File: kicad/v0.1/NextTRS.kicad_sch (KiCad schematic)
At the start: 62 parts, among them J1 TRS-80 M3 Pin Header, J10 DB15_Female_HighDensity, J2 TRS-80 M1 Pin Connector, J3 TRS-80 M3 Edge Connector, J4 TRS-80 M1 Edge Connector, J5 AudioJack3, J6 Mini-DIN-6, J7 USB_B_Micro, J8 SD_Card, J9 Programmer, Q1 2N7002, Q2 2N7002, Q3 2N7002, Q4 MMBT3904, Q5 MMBT3904, SW1 SW_DIP_x04, SW2 SW_Push, SW3 SW_Push, SW4 ESP_RESET, SW5 PTRS_RESET, U1 ESP32-WROVER-B, U2 74LVC245, U3 74LVC245, U4 MCP43x1, U5 74LVC245, U6 74LVC245, U7 74LVC245

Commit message: Do not use Bank 4 (1.5V)
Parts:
- added C11: 0.1uF, Capacitor_SMD:C_0805_2012Metric_Pad1.18x1.45mm_HandSolder, symbol Device:C
- renumbered C5 to C1, C6 to C2, C1 to C3, C2 to C4, C8 to C5, C3 to C6, C4 to C7, C7 to C8, J9 to J5, J8 to J6, J5 to J7, J6 to J8, J7 to J9, R11 to R1, R1 to R10, R2 to R11, R3 to R12, R4 to R13, R18 to R14, R19 to R15, R17 to R16, R5 to R17, R6 to R18, R14 to R19, R12 to R2, R13 to R3, R7 to R4, R8 to R5, R15 to R6, R16 to R7, R9 to R8, R10 to R9, SW3 to SW1, SW4 to SW2, SW5 to SW3, SW2 to SW4, SW1 to SW5, U5 to U4, U6 to U5, U7 to U6, U4 to U7
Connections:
- net +3V3: now also C11.2
- net GND: now also C11.1
- net INT_OUT_N: now also Conn1.182 (D10); no longer Conn1.158 (E9)
- net WAIT_OUT_N: now also Conn1.180 (D11); no longer Conn1.160 (E8)

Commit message: Add hires interface for the M3
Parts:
- added C1: 100, Capacitor_SMD:C_0805_2012Metric_Pad1.18x1.45mm_HandSolder, symbol Device:C
- added J5, J6: Conn_01x06_Male, Connector_PinHeader_2.54mm:PinHeader_1x06_P2.54mm_Horizontal, symbol Connector:Conn_01x06_Male
- added R10, R8, R9: 10K, Resistor_SMD:R_0805_2012Metric_Pad1.20x1.40mm_HandSolder, symbol Device:R
- added R4, R5, R6, R7: 4K7, Resistor_SMD:R_0805_2012Metric_Pad1.20x1.40mm_HandSolder, symbol Device:R
- renumbered C9 to C10, C10 to C11, C11 to C12, C3 to C2, C4 to C3, C6 to C4, C7 to C5, C1 to C6, C2 to C7, C5 to C8, C8 to C9, J8 to J10, J9 to J11, J10 to J12, J5 to J8, J6 to J9, R10 to R11, R11 to R12, R12 to R13, R13 to R14, R4 to R15, R5 to R16, R8 to R17, R9 to R18, R6 to R19, R7 to R20, R14 to R21, R15 to R22, R16 to R23, R17 to R24, R18 to R25, R19 to R26, SW5 to SW1, SW1 to SW2, SW2 to SW3, SW3 to SW4, SW4 to SW5
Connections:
- net +3.3V: now also R4.1, R5.1, R6.1, R7.1
- net CONF_1: now also Conn1.153 (A6), R4.2; no longer Conn1.192 (R7)
- net CONF_2: now also Conn1.149 (A7), R5.2; no longer Conn1.194 (P7)
- net CONF_3: now also Conn1.147 (C6), R6.2; no longer Conn1.198 (M6)
- net CONF_4: now also Conn1.143 (B8), R7.2; no longer Conn1.200 (L8)
- net GND: now also C1.2, J5.1 (Pin_1), J5.3 (Pin_3), J5.5 (Pin_5), J6.1 (Pin_1), J6.3 (Pin_3), J6.5 (Pin_5), R10.2, R8.2, R9.2
- net VIDEOX: now reaches U5.13 (B5)
- net VIDEOX: now also Conn1.198 (M6)
- net VSYNCX: now reaches U5.14 (B4)
- net VSYNCX: now also Conn1.194 (P7)
- net HSYNCX: now reaches U5.15 (B3)
- net HSYNCX: now also Conn1.192 (R7)
- net HSYNC: now reaches U5.5 (A3)
- net HSYNC: now also J5.6 (Pin_6), R8.1
- net VSYNC: now reaches U5.6 (A4)
- net VSYNC: now also J5.4 (Pin_4), R9.1
- net VIDEO: now reaches U5.7 (A5)
- net VIDEO: now also J5.2 (Pin_2), R10.1
- net HSYNC_O: now reaches Conn1.183 (R9)
- net HSYNC_O: now also J6.6 (Pin_6)
- net VSYNC_O: now reaches Conn1.191 (N8)
- net VSYNC_O: now also J6.4 (Pin_4)
- net VIDEO_O: now reaches Conn1.193 (L9)
- net VIDEO_O: now also C1.1, J6.2 (Pin_2)
- no-connect marks 5 -> 13
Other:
- moved on the sheet: C2, C3, C4, C5, J10, J7, J9, R11, R12, R13, R14, R15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

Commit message: Add HDMI connector
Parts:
- removed C12: 0.1uF, Capacitor_SMD:C_0805_2012Metric_Pad1.18x1.45mm_HandSolder, symbol Device:C
- removed D1: LED_RCBG, LED_THT:LED_D5.0mm-4_RGB, symbol TRS-IO-M1-rescue:LED_RCBG-Device
- removed J12: DB15_Female_HighDensity, PocketTRS_Connectors:DB_15F-VGA, symbol Connector:DB15_Female_HighDensity
- removed SW2, SW5: SW_Push, Button_Switch_THT:SW_PUSH_6mm, symbol Switch:SW_Push
- removed U7: MCP43x1, Package_SO:TSSOP-20_4.4x6.5mm_P0.65mm, symbol MCP43X1:MCP43x1
- added C1, C2, C3, C4, C5, C6, C7, C8: 100n, Capacitor_SMD:C_0805_2012Metric_Pad1.18x1.45mm_HandSolder, symbol Device:C
- added D1: LED_RKBG, LED_THT:LED_D5.0mm-4_RGB, symbol Device:LED_RKBG
- added J7: HDMI_A, Connector_HDMI:HDMI_A_Molex_208658-1001_Horizontal, symbol Connector:HDMI_A
- added R10, R11, R4, R5, R6, R7, R8, R9: 50, Resistor_SMD:R_0805_2012Metric_Pad1.20x1.40mm_HandSolder, symbol Device:R
- added R28, R29: 4K7, Resistor_SMD:R_0805_2012Metric_Pad1.20x1.40mm_HandSolder, symbol Device:R
- J1: footprint Connector_PinSocket_2.54mm:PinSocket_2x25_P2.54mm_Vertical -> Connector_PinHeader_2.54mm:PinHeader_2x25_P2.54mm_Vertical
- J2: footprint Connector_PinSocket_2.54mm:PinSocket_2x20_P2.54mm_Vertical -> Connector_PinHeader_2.54mm:PinHeader_2x20_P2.54mm_Vertical
- renumbered C6 to C10, C7 to C11, C2 to C12, C3 to C13, C4 to C14, C5 to C15, C8 to C16, C9 to C17, C10 to C18, C11 to C19, C1 to C9, J7 to J10, J10 to J11, J11 to J12, Q4 to Q1, Q5 to Q2, Q1 to Q3, Q2 to Q4, Q3 to Q5, R8 to R12, R9 to R13, R10 to R14, R11 to R21, R12 to R22, R13 to R23, R14 to R24, R21 to R25, R22 to R27, R23 to R30, R24 to R31, R25 to R32, R4 to R33, R5 to R34, R6 to R35, R7 to R36, SW3 to SW1, SW4 to SW2, SW1 to SW3
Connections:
- net PTRS_RESET is gone; now on net BUTTON: R30.2, SW2.2, U1.7 (IO35)
- net VGA_BLUE is gone; now on net _A12: Conn1.34 (P16)
- net VGA_GREEN is gone; now on net _A10: Conn1.30 (P15)
- net VGA_HSYNC is gone; now on net _A15: Conn1.40 (N16)
- net VGA_VSYNC is gone; now on net _A13: Conn1.36 (N15)
- net +3.3V: now also R25.1, R27.1, R30.1, R10.1, R11.1, R4.1, R5.1, R6.1, R7.1, R8.1, R9.1; no longer R26.1
- net +3V3: now also R26.1, R28.1, R29.1; no longer R25.1, R27.1, R30.1, U5.1 (A->B)
- net A0: now also U2.9 (A7); no longer U2.2 (A0)
- net A1: now also U2.8 (A6); no longer U2.3 (A1)
- net A10: now also U4.18 (B0); no longer U4.4 (A2)
- net A11: now also U4.13 (B5); no longer U4.5 (A3)
- net A12: now also U4.17 (B1); no longer U4.6 (A4)
- net A13: now also U4.16 (B2); no longer U4.7 (A5)
- net A14: now also U4.14 (B4); no longer U4.8 (A6)
- net A15: now also U4.15 (B3); no longer U4.9 (A7)
- net A2: now also U2.7 (A5); no longer U2.4 (A2)
- net A3: now also U2.6 (A4); no longer U2.5 (A3)
- net A4: now also U2.5 (A3); no longer U2.6 (A4)
- net A5: now also U2.4 (A2); no longer U2.7 (A5)
- net A6: now also U2.3 (A1); no longer U2.8 (A6)
- net A7: now also U2.2 (A0); no longer U2.9 (A7)
- net A8: now also U4.12 (B6); no longer U4.2 (A0)
- net A9: now also U4.11 (B7); no longer U4.3 (A1)
- net ABUS_DIR: now also Conn1.57 (R11); no longer Conn1.75 (M14), U4.1 (A->B)
- net ABUS_EN: now also Conn1.59 (T12); no longer Conn1.73 (M15)
- net BUTTON: no longer R26.2, U1.5 (IO39)
- net CASS_OUT: now also Conn1.135 (C10); no longer Conn1.70 (H15)
- net CS_FPGA: now also Conn1.76 (K11); no longer Conn1.42 (N14)
- net CTRL1_EN: now also Conn1.182 (D10); no longer Conn1.154 (J11)
- net CTRL_DIR: now also Conn1.27 (T6); no longer Conn1.148 (A9)
- net CTRL_EN: now also Conn1.29 (P6); no longer Conn1.152 (L12)
- net D0: now also U6.9 (A7); no longer U6.2 (A0)
- net D1: now also U6.8 (A6); no longer U6.3 (A1)
- net D2: now also U6.7 (A5); no longer U6.4 (A2)
- net D3: now also U6.6 (A4); no longer U6.5 (A3)
- net D4: now also U6.5 (A3); no longer U6.6 (A4)
- net D5: now also U6.4 (A2); no longer U6.7 (A5)
- net D6: now also U6.3 (A1); no longer U6.8 (A6)
- net D7: now also U6.2 (A0); no longer U6.9 (A7)
- net DBUS_DIR: now also Conn1.81 (T15); no longer Conn1.101 (E15)
- net DBUS_EN: now also Conn1.83 (J16); no longer Conn1.97 (F16)
- net DONE: now also Conn1.130 (E15); no longer Conn1.68 (G16)
- net ESP_S0: now also Conn1.86 (J12); no longer Conn1.52 (K14)
- net ESP_S1: now also Conn1.90 (H12); no longer Conn1.56 (K16)
- net ESP_S2: now also Conn1.92 (G11); no longer Conn1.58 (J15)
- net ESP_S3: now also Conn1.96 (B10); no longer Conn1.62 (H16)
- net EXTIOSEL: now also Conn1.154 (J11); no longer Conn1.140 (D16)
- net GND: now also Conn1.26 (GND), U5.1 (A->B), D1.2 (K), J7.17 (GND)
- net HSYNCX: now also Conn1.198 (M6); no longer Conn1.192 (R7)
- net HSYNC_O: now also Conn1.177 (N7); no longer Conn1.183 (R9)
- net INT: now also Conn1.180 (D11); no longer Conn1.146 (C9)
- net IN_N: now also U3.9 (A7); no longer U3.4 (A2)
- net IOREQ_N: now also U3.5 (A3); no longer U3.7 (A5)
- net M1_N: now also U3.6 (A4); no longer U3.8 (A6)
- net MISO: now also Conn1.80 (K13); no longer Conn1.46 (L14)
- net MOSI: now also Conn1.84 (H13); no longer Conn1.50 (K15)
- net OUT_N: now also U3.8 (A6); no longer U3.3 (A1)
- net RAS_N: now also U3.4 (A2); no longer U3.2 (A0)
- net RD_N: now also U3.2 (A0); no longer U3.5 (A3)
- net REQ: now also Conn1.98 (A13); no longer Conn1.64 (H14)
- net RESET_N: now also U3.7 (A5); no longer U3.9 (A7)
- net SCK: now also Conn1.78 (K12); no longer Conn1.44 (L16)
- net VIDEOX: now also Conn1.193 (L9); no longer Conn1.198 (M6)
- net VIDEO_O: now also Conn1.191 (N8); no longer Conn1.193 (L9)
- net VSYNCX: now also Conn1.200 (L8); no longer Conn1.194 (P7)
- net VSYNC_O: now also Conn1.183 (R9); no longer Conn1.191 (N8)
- net WAIT: now also Conn1.176 (F10); no longer Conn1.142 (E14)
- net WR_N: now also U3.3 (A1); no longer U3.6 (A4)
- net _A0: now also Conn1.79 (G12), U2.11 (B7); no longer Conn1.27 (T6), U2.18 (B0)
- net _A1: now also Conn1.77 (F13), U2.12 (B6); no longer Conn1.29 (P6), U2.17 (B1)
- net _A10: now also U4.2 (A0); no longer Conn1.57 (R11), U4.16 (B2)
- net _A11: now also Conn1.44 (L16), U4.7 (A5); no longer Conn1.59 (T12), U4.15 (B3)
- net _A12: now also U4.3 (A1); no longer Conn1.63 (R12), U4.14 (B4)
- net _A13: now also U4.4 (A2); no longer Conn1.65 (P13), U4.13 (B5)
- net _A14: now also Conn1.42 (N14), U4.6 (A4); no longer Conn1.67 (R13), U4.12 (B6)
- net _A15: now also U4.5 (A3); no longer Conn1.69 (T14), U4.11 (B7)
- net _A2: now also Conn1.75 (M14), U2.13 (B5); no longer Conn1.33 (T7), U2.16 (B2)
- net _A3: now also Conn1.73 (M15), U2.14 (B4); no longer Conn1.35 (R8), U2.15 (B3)
- net _A4: now also Conn1.69 (T14), U2.15 (B3); no longer Conn1.39 (T8), U2.14 (B4)
- net _A5: now also Conn1.67 (R13), U2.16 (B2); no longer Conn1.41 (P8), U2.13 (B5)
- net _A6: now also Conn1.65 (P13), U2.17 (B1); no longer Conn1.45 (T9), U2.12 (B6)
- net _A7: now also Conn1.63 (R12), U2.18 (B0); no longer Conn1.47 (P9), U2.11 (B7)
- net _A8: now also Conn1.46 (L14), U4.8 (A6); no longer Conn1.51 (P11), U4.18 (B0)
- net _A9: now also Conn1.74 (L13), U4.9 (A7); no longer Conn1.53 (T11), U4.17 (B1)
- net _D0: now also Conn1.107 (A15), U6.11 (B7); no longer Conn1.77 (F13), U6.18 (B0)
- net _D1: now also Conn1.103 (D14), U6.12 (B6); no longer Conn1.79 (G12), U6.17 (B1)
- net _D2: now also Conn1.101 (E15), U6.13 (B5); no longer Conn1.81 (T15), U6.16 (B2)
- net _D3: now also Conn1.97 (F16), U6.14 (B4); no longer Conn1.83 (J16), U6.15 (B3)
- net _D4: now also Conn1.95 (F14), U6.15 (B3); no longer Conn1.85 (J14), U6.14 (B4)
- net _D5: now also Conn1.91 (G15), U6.16 (B2); no longer Conn1.89 (G14), U6.13 (B5)
- net _D6: now also Conn1.89 (G14), U6.17 (B1); no longer Conn1.91 (G15), U6.12 (B6)
- net _D7: now also Conn1.85 (J14), U6.18 (B0); no longer Conn1.95 (F14), U6.11 (B7)
- net _IN_N: now also Conn1.53 (T11), U3.11 (B7); no longer Conn1.113 (A14), U3.16 (B2)
- net _IOREQ_N: now also Conn1.41 (P8), U3.15 (B3); no longer Conn1.121 (B12), U3.13 (B5)
- net _M1_N: now also Conn1.45 (T9), U3.14 (B4); no longer Conn1.123 (A12), U3.12 (B6)
- net _OUT_N: now also Conn1.51 (P11), U3.12 (B6); no longer Conn1.109 (B14), U3.17 (B1)
- net _RAS_N: now also Conn1.39 (T8), U3.16 (B2); no longer Conn1.107 (A15), U3.18 (B0)
- net _RD_N: now also Conn1.33 (T7), U3.18 (B0); no longer Conn1.115 (B13), U3.15 (B3)
- net _RESET_N: now also Conn1.47 (P9), U3.13 (B5); no longer Conn1.125 (C11), U3.11 (B7)
- net _WR_N: now also Conn1.35 (R8), U3.17 (B1); no longer Conn1.119 (C12), U3.14 (B4)
- net at R1.2: now also D1.1 (RA)
- net at R3.2: now also D1.3 (BA)
- net at R2.2: now also D1.4 (GA)
- net EXTIOSEL_IN_N: now reaches Conn1.186 (E10)
- net EXTIOSEL_IN_N: now also U5.2 (A0), R29.2
- net CS43x1: no longer names the net of U1.26 (IO4)
- removed net EXTIOSEL_OUT_N: Conn1.176 (F10), U5.2 (A0)
- net INT_OUT_N renamed INT_IN_N
- net INT_IN_N: now also Conn1.194 (P7), R26.2; no longer Conn1.182 (D10)
- net VGA_RED renamed ABUS_DIR_N
- net ABUS_DIR_N: now also U4.1 (A->B)
- net WAIT_OUT_N renamed WAIT_IN_N
- net WAIT_IN_N: now also Conn1.192 (R7), R28.2; no longer Conn1.180 (D11)
- new net: C2.2, J7.3 (D2-)
- new net: C6.2, J7.9 (D0-)
- new net: C7.2, J7.10 (CK+)
- new net: C1.2, J7.1 (D2+)
- new net: C8.2, J7.12 (CK-)
- new net: C3.2, J7.4 (D1+)
- new net: C4.2, J7.6 (D1-)
- new net: C5.2, J7.7 (D0+)
- new net HDMI_TX0_N: C6.1, Conn1.62 (H16), R9.2
- new net HDMI_TX0_P: C5.1, Conn1.64 (H14), R8.2
- new net HDMI_TX1_N: C4.1, Conn1.56 (K16), R7.2
- new net HDMI_TX1_P: C3.1, Conn1.58 (J15), R6.2
- new net HDMI_TX2_N: C2.1, Conn1.50 (K15), R5.2
- new net HDMI_TX2_P: C1.1, Conn1.52 (K14), R4.2
- new net HDMI_TXC_N: C8.1, Conn1.70 (H15), R11.2
- new net HDMI_TXC_P: C7.1, Conn1.68 (G16), R10.2
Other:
- moved on the sheet: C12, C13, C14, C15, C18, C9, J10, J5, J6, Q3, Q4, Q5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

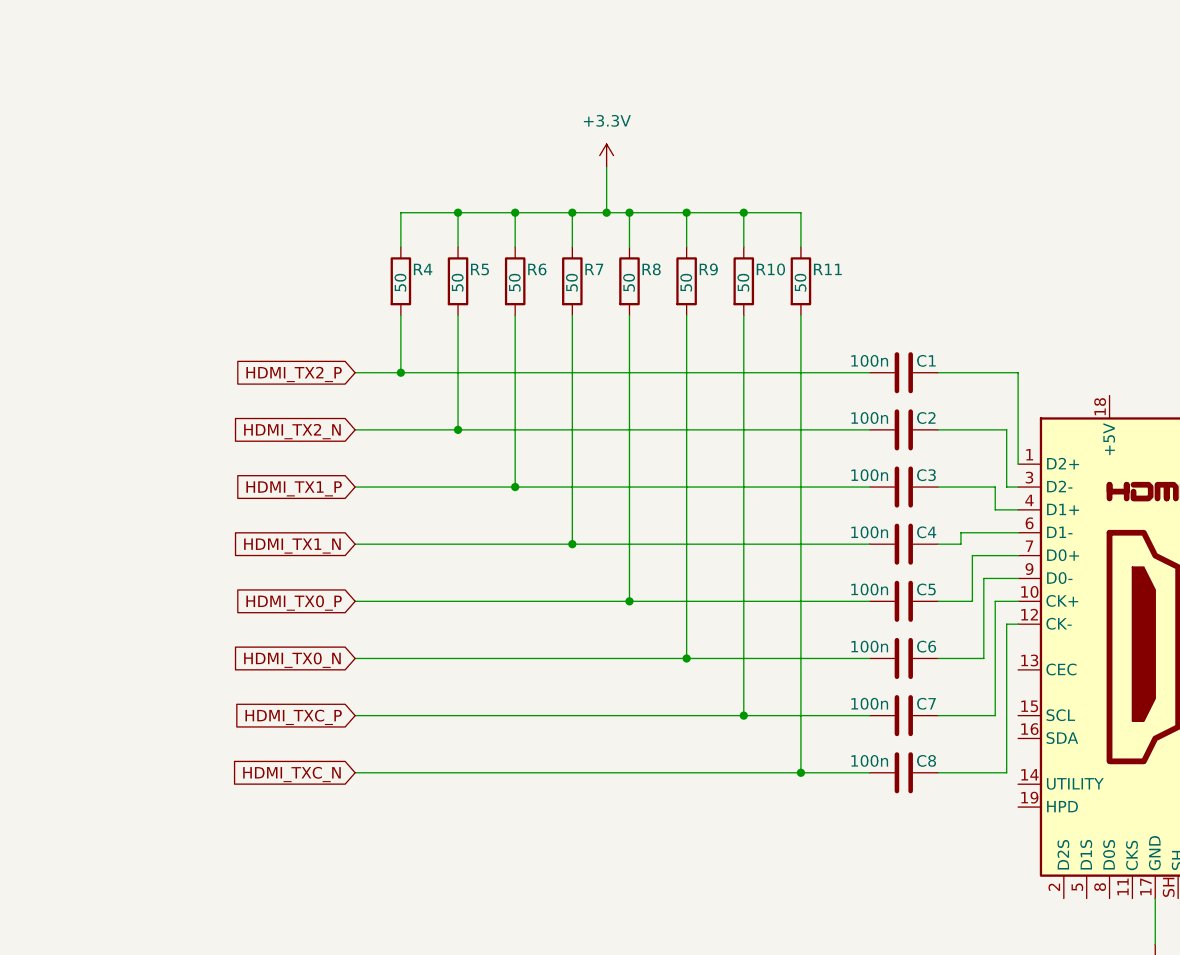
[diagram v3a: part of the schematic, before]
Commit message: HDMI: move resistors before caps
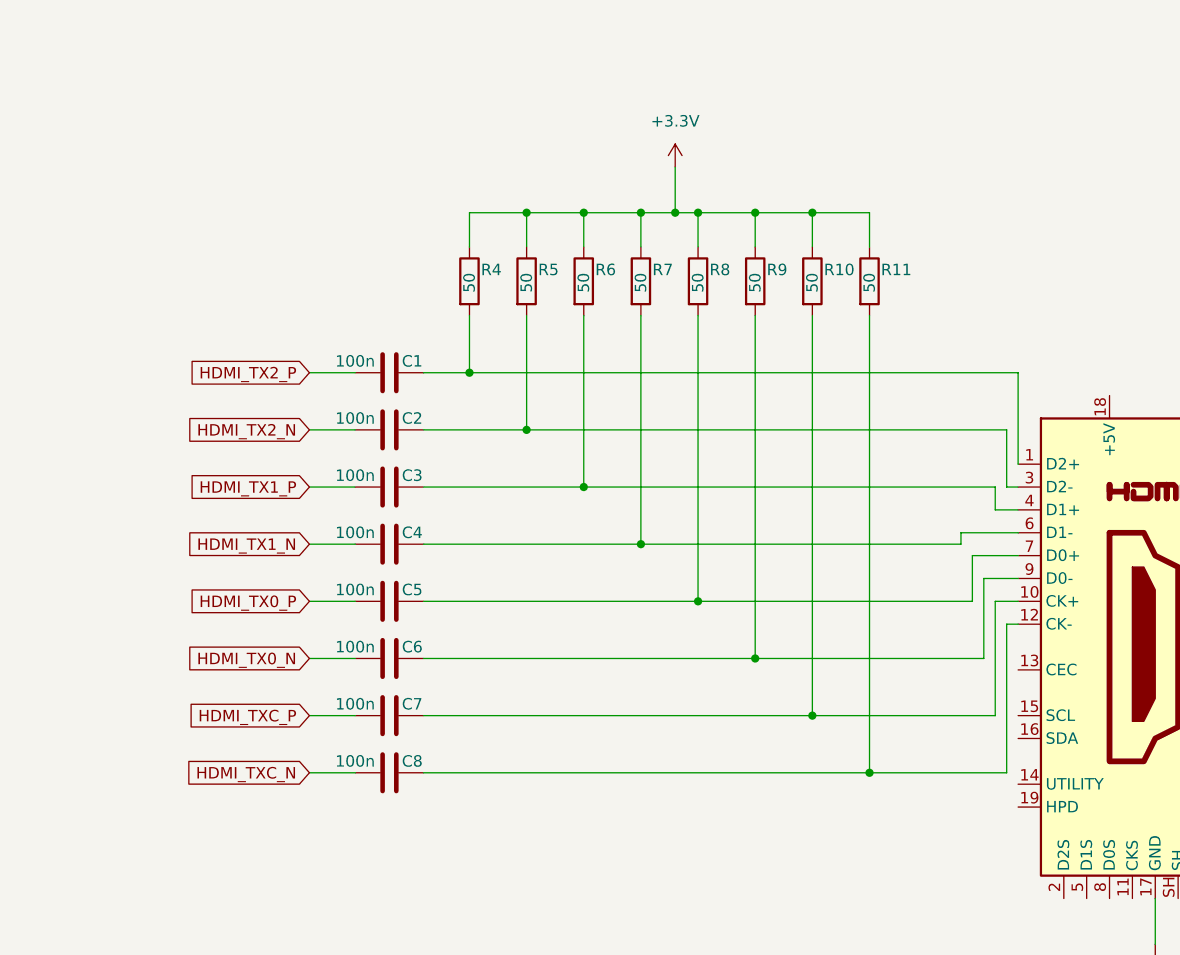
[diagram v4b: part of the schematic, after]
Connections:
- net HDMI_TX0_N: no longer R9.2
- net HDMI_TX0_P: no longer R8.2
- net HDMI_TX1_N: no longer R7.2
- net HDMI_TX1_P: no longer R6.2
- net HDMI_TX2_N: no longer R5.2
- net HDMI_TX2_P: no longer R4.2
- net HDMI_TXC_N: no longer R11.2
- net HDMI_TXC_P: no longer R10.2
- net at C2.2, J7.3 (D2-): now also R5.2
- net at C6.2, J7.9 (D0-): now also R9.2
- net at C7.2, J7.10 (CK+): now also R10.2
- net at C1.2, J7.1 (D2+): now also R4.2
- net at C8.2, J7.12 (CK-): now also R11.2
- net at C3.2, J7.4 (D1+): now also R6.2
- net at C4.2, J7.6 (D1-): now also R7.2
- net at C5.2, J7.7 (D0+): now also R8.2
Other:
- moved on the sheet: C1, C2, C3, C4, C5, C6, C7, C8, R10, R11, R4, R5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

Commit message: Move LED to FPGA. Add JTAG interface
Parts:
- SW2: value PTRS_RESET -> PTRS_RESET/STATUS
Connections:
- net CONF_1: now also Conn1.131 (A11); no longer Conn1.153 (A6)
- net CONF_2: now also Conn1.129 (B11); no longer Conn1.149 (A7)
- net CONF_3: now also Conn1.125 (C11); no longer Conn1.147 (C6)
- net CONF_4: now also Conn1.123 (A12); no longer Conn1.143 (B8)
- net LED_BLUE: now also Conn1.142 (E14); no longer U1.29 (IO5)
- net LED_GREEN: now also Conn1.140 (D16); no longer U1.37 (IO23)
- net LED_RED: now also Conn1.146 (C9); no longer U1.12 (IO27)
- net RXD0: now also Conn1.147 (C6)
- net TXD0: now also Conn1.153 (A6)
- new net JTAG_TCK: Conn1.149 (A7), U1.37 (IO23)
- new net JTAG_TMS: Conn1.143 (B8), U1.29 (IO5)
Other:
- note added: "JTAG_TDI"
- note added: "JTAG_TDO"
- moved on the sheet: R30

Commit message: Updated schematics to facilitate routing
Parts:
- added D2, D3, D4, D5: LED, LED_SMD:LED_0805_2012Metric_Pad1.15x1.40mm_HandSolder, symbol Device:LED
- added R37, R38, R39, R40: 100, Resistor_SMD:R_0805_2012Metric_Pad1.20x1.40mm_HandSolder, symbol Device:R
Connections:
- net +3.3V: no longer Conn1.22 (3V3), Conn1.24 (3V3), R33.1, R34.1, R35.1, R36.1, U1.2 (3.3V)
- net +3V3: now also C18.1, Conn1.22 (3V3), Conn1.24 (3V3), R33.1, R34.1, R35.1, R36.1, U1.2 (3.3V), U5.1 (A->B); no longer C18.2
- net A10: now also U4.11 (B7); no longer U4.18 (B0)
- net A11: now also U4.16 (B2); no longer U4.13 (B5)
- net A12: now also U4.12 (B6); no longer U4.17 (B1)
- net A13: now also U4.13 (B5); no longer U4.16 (B2)
- net A14: now also U4.15 (B3); no longer U4.14 (B4)
- net A15: now also U4.14 (B4); no longer U4.15 (B3)
- net A8: now also U4.17 (B1); no longer U4.12 (B6)
- net A9: now also U4.18 (B0); no longer U4.11 (B7)
- net CONF_1: now also Conn1.123 (A12); no longer Conn1.131 (A11)
- net CONF_2: now also Conn1.125 (C11); no longer Conn1.129 (B11)
- net CONF_3: now also Conn1.129 (B11); no longer Conn1.125 (C11)
- net CONF_4: now also Conn1.131 (A11); no longer Conn1.123 (A12)
- net CTRL1_EN: now also Conn1.192 (R7); no longer Conn1.182 (D10)
- net EXTIOSEL: now also Conn1.180 (D11); no longer Conn1.154 (J11)
- net EXTIOSEL_IN_N: now also Conn1.194 (P7), R26.2, U5.18 (B0); no longer Conn1.186 (E10), R29.2, U5.2 (A0)
- net EXTIOSEL_N: now also U5.2 (A0); no longer U5.18 (B0)
- net GND: now also C18.2, R37.2, R38.2, R39.2, R40.2; no longer C18.1, U5.1 (A->B)
- net HDMI_TX0_N: now also Conn1.64 (H14); no longer Conn1.62 (H16)
- net HDMI_TX0_P: now also Conn1.62 (H16); no longer Conn1.64 (H14)
- net HDMI_TX1_N: now also Conn1.58 (J15); no longer Conn1.56 (K16)
- net HDMI_TX1_P: now also Conn1.56 (K16); no longer Conn1.58 (J15)
- net HDMI_TX2_N: now also Conn1.52 (K14); no longer Conn1.50 (K15)
- net HDMI_TX2_P: now also Conn1.50 (K15); no longer Conn1.52 (K14)
- net HSYNC: now also U5.15 (B3); no longer U5.5 (A3)
- net HSYNCX: now also Conn1.182 (D10), U5.5 (A3); no longer Conn1.198 (M6), U5.15 (B3)
- net HSYNC_O: now also Conn1.183 (R9); no longer Conn1.177 (N7)
- net INT: now also Conn1.154 (J11); no longer Conn1.180 (D11)
- net INT_IN_N: now also Conn1.200 (L8), R29.2, U5.16 (B2); no longer Conn1.194 (P7), R26.2, U5.4 (A2)
- net INT_N: now also U5.4 (A2); no longer U5.16 (B2)
- net IN_N: now also U3.2 (A0); no longer U3.9 (A7)
- net IOREQ_N: now also U3.7 (A5); no longer U3.5 (A3)
- net LED_BLUE: now also Conn1.148 (A9); no longer Conn1.142 (E14)
- net LED_GREEN: now also Conn1.146 (C9); no longer Conn1.140 (D16)
- net LED_RED: now also Conn1.152 (L12); no longer Conn1.146 (C9)
- net M1_N: now also U3.8 (A6); no longer U3.6 (A4)
- net OUT_N: now also U3.5 (A3); no longer U3.8 (A6)
- net RAS_N: now also U3.6 (A4); no longer U3.4 (A2)
- net RD_N: now also U3.3 (A1); no longer U3.2 (A0)
- net RESET_N: now also U3.9 (A7); no longer U3.7 (A5)
- net VIDEO: now also U5.13 (B5); no longer U5.7 (A5)
- net VIDEOX: now also Conn1.177 (N7), U5.7 (A5); no longer Conn1.193 (L9), U5.13 (B5)
- net VIDEO_O: now also Conn1.193 (L9); no longer Conn1.191 (N8)
- net VSYNC: now also U5.14 (B4); no longer U5.6 (A4)
- net VSYNCX: now also Conn1.186 (E10), U5.6 (A4); no longer Conn1.200 (L8), U5.14 (B4)
- net VSYNC_O: now also Conn1.191 (N8); no longer Conn1.183 (R9)
- net WAIT_IN_N: now also Conn1.198 (M6), U5.17 (B1); no longer Conn1.192 (R7), U5.3 (A1)
- net WAIT_N: now also U5.3 (A1); no longer U5.17 (B1)
- net WR_N: now also U3.4 (A2); no longer U3.3 (A1)
- net _A10: now also Conn1.46 (L14), U4.9 (A7); no longer Conn1.30 (P15), U4.2 (A0)
- net _A11: now also Conn1.34 (P16), U4.4 (A2); no longer Conn1.44 (L16), U4.7 (A5)
- net _A12: now also Conn1.44 (L16), U4.8 (A6); no longer Conn1.34 (P16), U4.3 (A1)
- net _A13: now also Conn1.42 (N14), U4.7 (A5); no longer Conn1.36 (N15), U4.4 (A2)
- net _A14: now also Conn1.36 (N15), U4.5 (A3); no longer Conn1.42 (N14), U4.6 (A4)
- net _A15: now also U4.6 (A4); no longer U4.5 (A3)
- net _A8: now also Conn1.30 (P15), U4.3 (A1); no longer Conn1.46 (L14), U4.8 (A6)
- net _A9: now also U4.2 (A0); no longer U4.9 (A7)
- net _IN_N: now also Conn1.33 (T7), U3.18 (B0); no longer Conn1.53 (T11), U3.11 (B7)
- net _IOREQ_N: now also Conn1.47 (P9), U3.13 (B5); no longer Conn1.41 (P8), U3.15 (B3)
- net _M1_N: now also Conn1.51 (P11), U3.12 (B6); no longer Conn1.45 (T9), U3.14 (B4)
- net _OUT_N: now also Conn1.41 (P8), U3.15 (B3); no longer Conn1.51 (P11), U3.12 (B6)
- net _RAS_N: now also Conn1.45 (T9), U3.14 (B4); no longer Conn1.39 (T8), U3.16 (B2)
- net _RD_N: now also Conn1.35 (R8), U3.17 (B1); no longer Conn1.33 (T7), U3.18 (B0)
- net _RESET_N: now also Conn1.53 (T11), U3.11 (B7); no longer Conn1.47 (P9), U3.13 (B5)
- net _WR_N: now also Conn1.39 (T8), U3.16 (B2); no longer Conn1.35 (R8), U3.17 (B1)
- net D0+: now reaches C5.2, J7.7 (D0+), R8.2
- net D2-: now reaches C2.2, J7.3 (D2-), R5.2
- net D0-: now reaches C6.2, J7.9 (D0-), R9.2
- net CK+: now reaches C7.2, J7.10 (CK+), R10.2
- net D2+: now reaches C1.2, J7.1 (D2+), R4.2
- net CK-: now reaches C8.2, J7.12 (CK-), R11.2
- net D1+: now reaches C3.2, J7.4 (D1+), R6.2
- net D1-: now reaches C4.2, J7.6 (D1-), R7.2
- net LED4: now reaches Conn1.132 (F15)
- net LED4: now also D5.2 (A)
- net LED3: now reaches Conn1.136 (C13)
- net LED3: now also D4.2 (A)
- new net: D2.1 (K), R37.1
- new net: D4.1 (K), R39.1
- new net: D5.1 (K), R40.1
- new net: D3.1 (K), R38.1
- new net LED1: Conn1.142 (E14), D2.2 (A)
- new net LED2: Conn1.140 (D16), D3.2 (A)
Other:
- moved on the sheet: C18, R26, R28, R29
